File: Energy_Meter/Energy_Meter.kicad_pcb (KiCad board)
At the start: 2 copper layers, 45.7 x 39.6 mm, 37 parts, among them J1 RJ45, P1 SHUNT, P2 HV, U1 MCP6V27, U2 MAX11644, U3 CRE1S0505S3C, U4 ADUM1250ARZ, U5 MCP2551-I/P, U6 7805, U7 Kitprog-PSoC

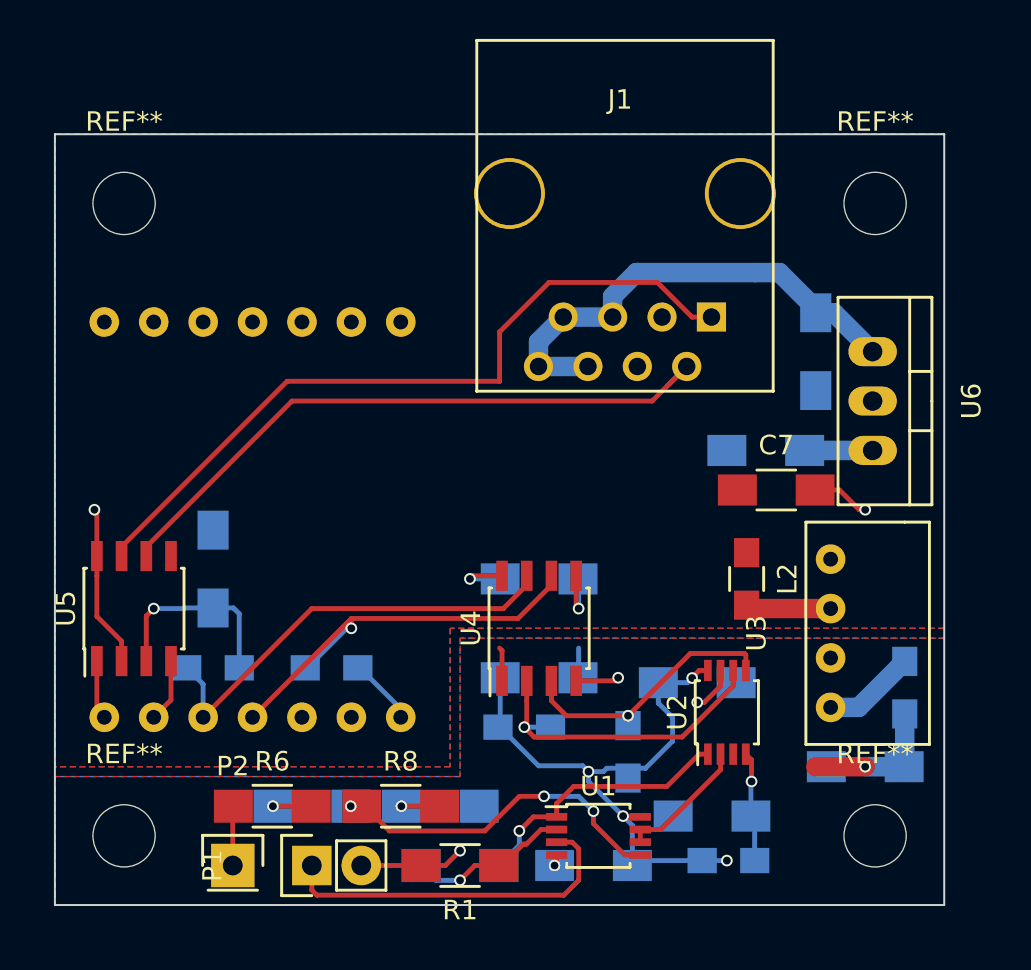
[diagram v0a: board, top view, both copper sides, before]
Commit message: Energy Meter tweaks
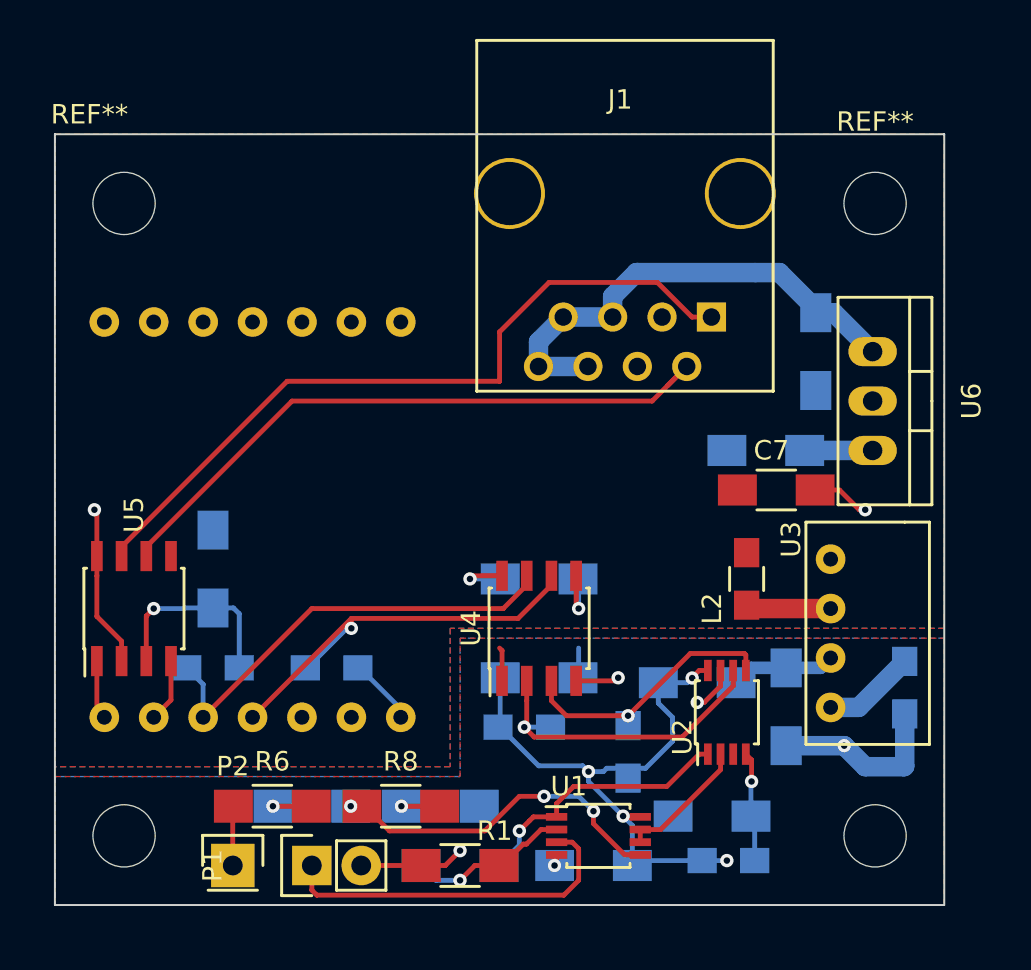
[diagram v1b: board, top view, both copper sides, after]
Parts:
- moved C3 5.10 mm to (193.0, 115.3), turned to 90 degrees
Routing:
- net GNDD: track 12.4 -> 17.7 mm
- net VCC: track 40.9 -> 42.9 mm
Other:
- net class Default: clearance 0.2 -> 0.1524; trace_width 0.25 -> 0.1524; via_dia 0.6 -> 0.6858; via_drill 0.4 -> 0.3302
- rule trace_clearance: 0.2 -> 0.1524
- rule trace_min: 0.2 -> 0.1524
- rule via_min_drill: 0.3 -> 0.3302
- rule via_min_size: 0.4 -> 0.6858

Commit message: Energy Meter is *more* done
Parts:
- removed J1: RJ45, Connect:RJ45_8
- removed the REF** at (197.6, 89.4)
- removed the REF** at (159.0, 89.4)
- removed the REF** at (197.6, 121.9)
- removed the REF** at (159.0, 121.9)
- added G***: LOGO, UNCAMotorsports:UNCA Logo, F.Cu at (170.7, 89.3)
- added GND: Pin_Header_Straight_1x01, Pin_Headers:Pin_Header_Straight_1x01, F.Cu at (193.2, 88.5)
- added P3: CONN_02X04, Connectors_Molex:Molex_NanoFit_2x04x2.50mm_Straight, F.Cu at (189.2, 88.9)
- added REF**: MountingHole_3mm, Mounting_Holes:MountingHole_3mm, F.Cu at (158.8, 122.2)
- added REF**: MountingHole_3mm, Mounting_Holes:MountingHole_3mm, F.Cu at (197.9, 122.2)
- added REF**: MountingHole_3mm, Mounting_Holes:MountingHole_3mm, F.Cu at (197.9, 89.2)
- added REF**: MountingHole_3mm, Mounting_Holes:MountingHole_3mm, F.Cu at (158.8, 89.2)
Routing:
- net +12V: track 31.0 -> 18.4 mm
- net VCC: track 42.9 -> 45.9 mm, vias 5 -> 8
- net /CANH: track 38.7 -> 41.6 mm, vias 0 -> 2
- net /CANL: track 33.5 -> 33.7 mm, vias 0 -> 2
